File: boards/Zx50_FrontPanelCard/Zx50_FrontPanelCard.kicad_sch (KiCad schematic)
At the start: 22 parts, among them J1 Zx50_EdgeConnector, J2 FrontPanelConnect, J3 Front Panel 2, J4 Front Panel, U1 74LVC573, U2 AMS1117-3.3, U3 74LVC573, U4 74LVC573, U5 74LVC573, U6 74LVC573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

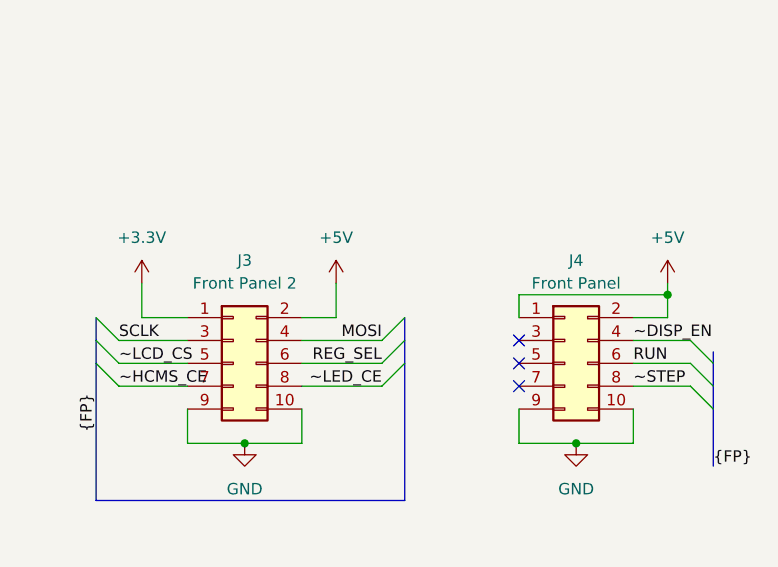
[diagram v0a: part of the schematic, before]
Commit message: Lots of updates: Work on memory card Rev C with Lattice XO3LF, finish up the front panel card firmware for the pico., add some results for the clock mezzanine Rev B.
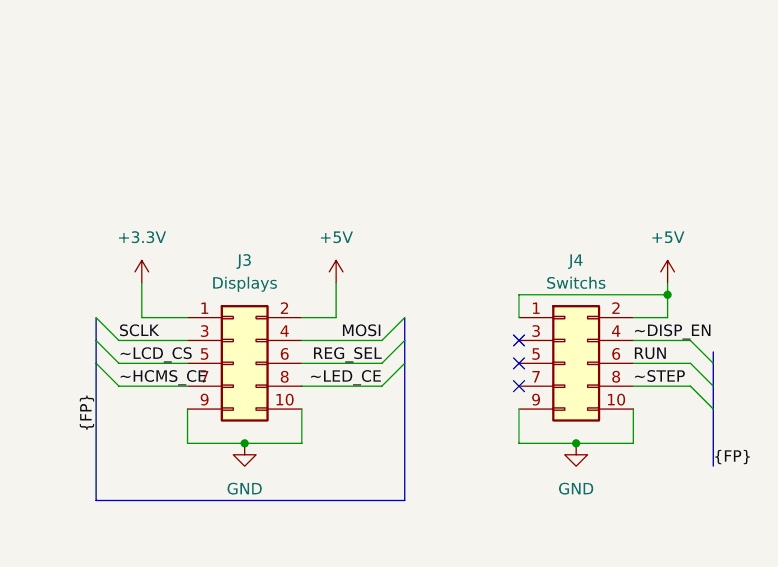
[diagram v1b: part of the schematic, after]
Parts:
- J3: value Front Panel 2 -> Displays
- J4: value Front Panel -> Switchs
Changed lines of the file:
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@@
 			)
 		)
-		(property "Value" "Front Panel 2"
+		(property "Value" "Displays"
 			(at 229.87 43.18 0)
 			(effects
@@
 			)
 		)
-		(property "Value" "Front Panel"
+		(property "Value" "Switchs"
 			(at 266.7 43.18 0)
 			(effects
